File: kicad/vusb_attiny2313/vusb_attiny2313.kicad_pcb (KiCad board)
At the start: 2 copper layers, 38 parts, among them J1 USB, Q1 BSS138, Q2 BSS138, SW2 SW_DIP_x03, U1 74HC595, U2 ATTINY2313-20PU, U3 74HC595, U4 74HC595, U5 27C256, U6 LT1073CS, Y1 12Mhz

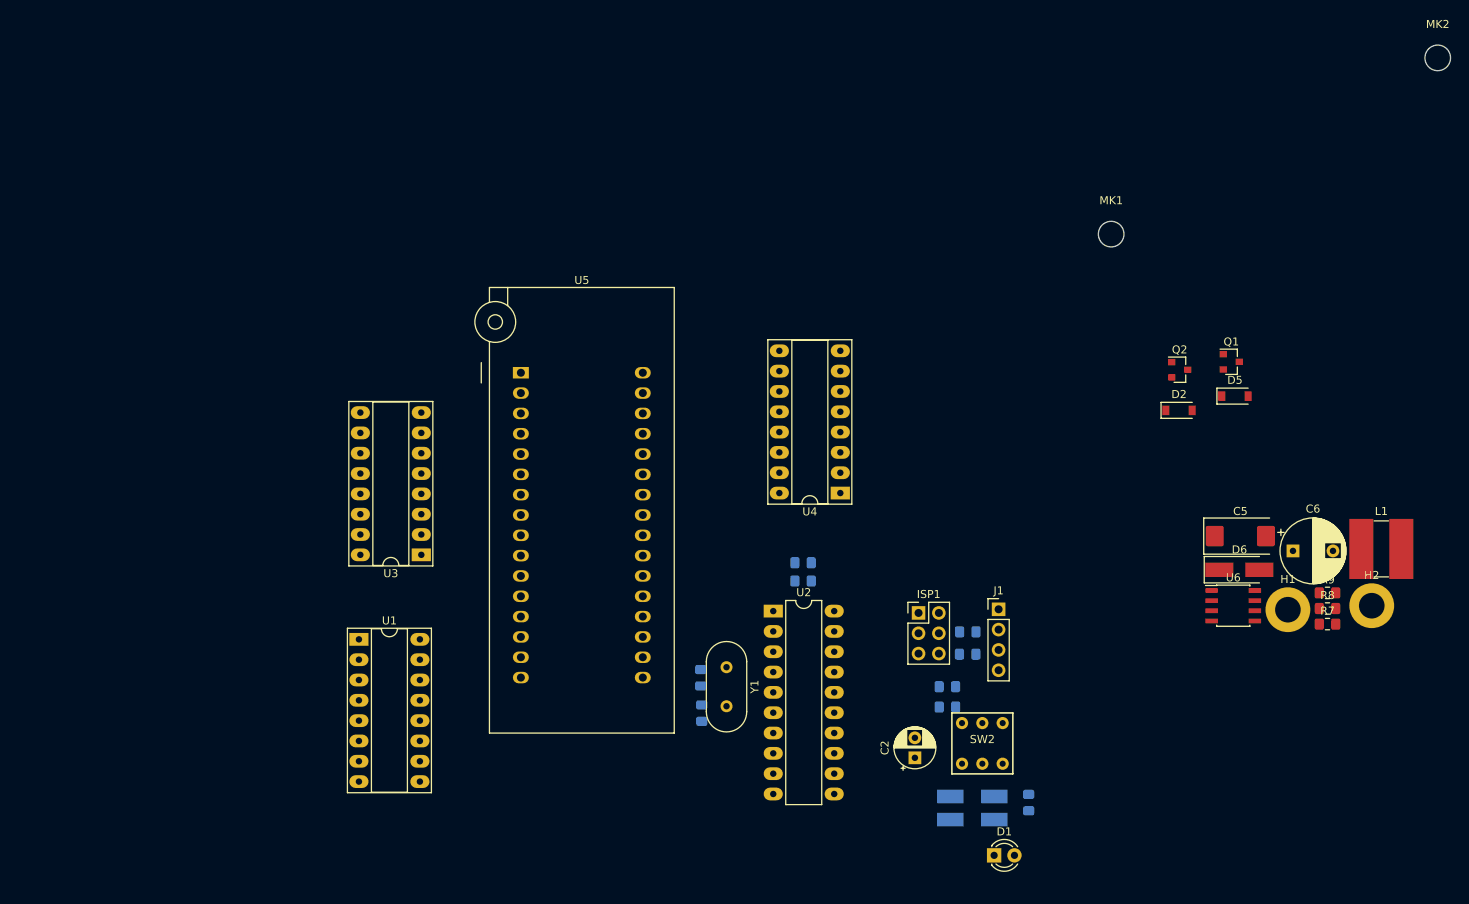
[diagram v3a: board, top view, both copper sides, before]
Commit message: fuses angepasst!
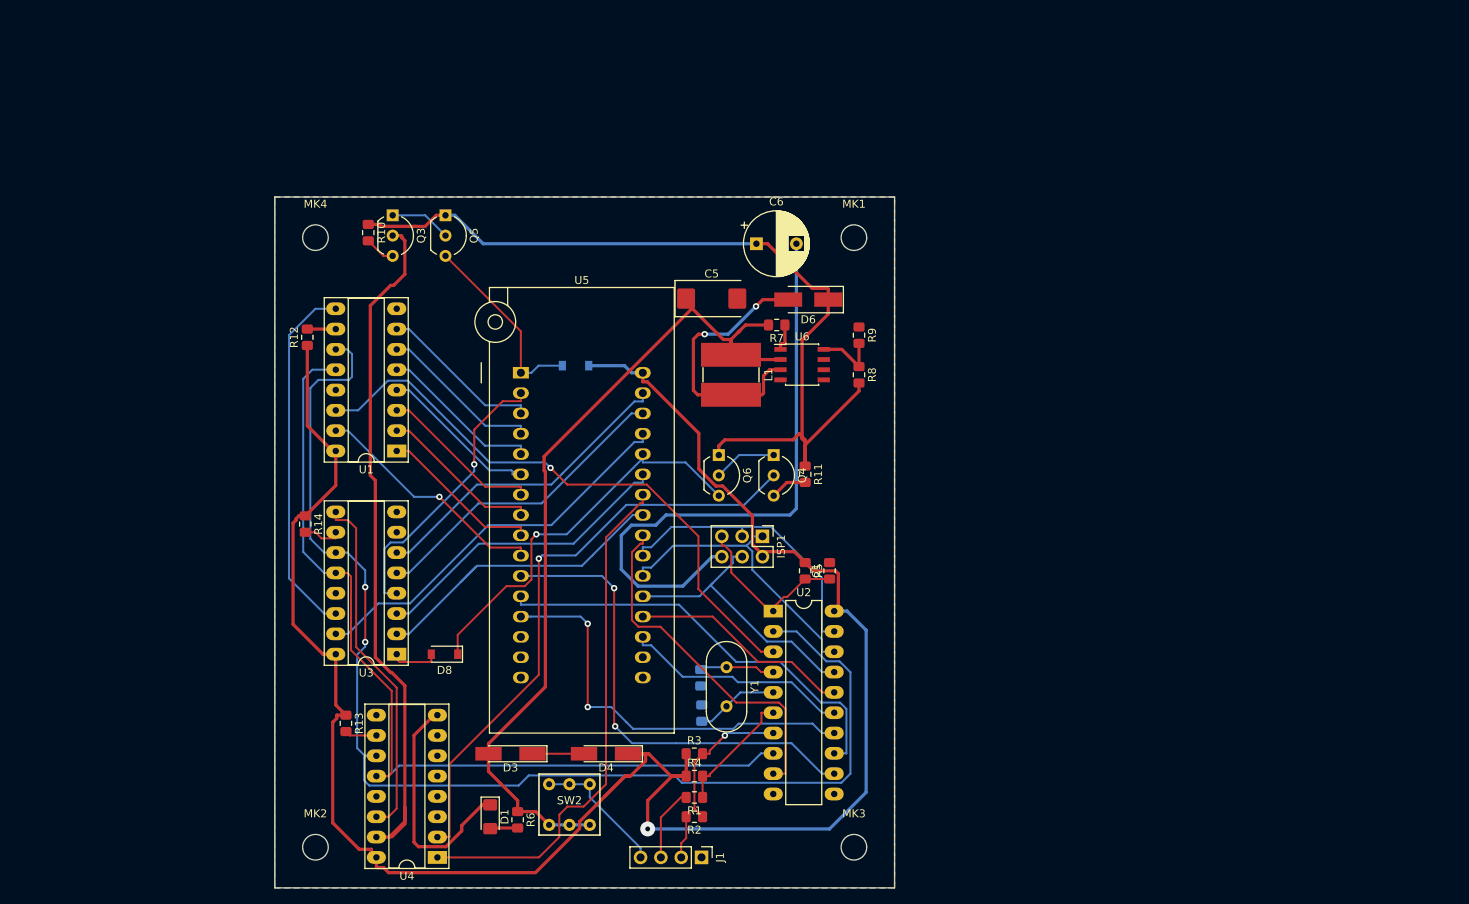
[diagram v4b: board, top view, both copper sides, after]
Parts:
- removed C2: 10µ, Capacitor_THT:CP_Radial_D5.0mm_P2.50mm
- removed D2, D5: SD 103BW, Diode_SMD:D_SOD-123
- removed H1, H2: MH, MountingHole:MountingHole_3.2mm_M3_DIN965_Pad
- removed Q1, Q2: BSS138, Package_TO_SOT_SMD:SOT-23
- added D7: SD 103BW, Diode_SMD:D_SOD-123, B.Cu at (99.8, 42.7)
- added D8: SD 103BW, Diode_SMD:D_SOD-123, F.Cu at (83.4, 78.7)
- added MK3: Mounting_Hole, MountingHole:MountingHole_3.2mm_M3, F.Cu at (134.6, 102.9)
- added MK4: Mounting_Hole, MountingHole:MountingHole_3.2mm_M3, F.Cu at (67.3, 26.7)
- added Q3: 2N3904, Package_TO_SOT_THT:TO-92_Inline_Wide, F.Cu at (77.0, 23.9)
- added Q4: 2N3904, Package_TO_SOT_THT:TO-92_Inline_Wide, F.Cu at (124.6, 53.8)
- added Q5: 2N3906, Package_TO_SOT_THT:TO-92_Inline_Wide, F.Cu at (83.6, 23.9)
- added Q6: 2N3906, Package_TO_SOT_THT:TO-92_Inline_Wide, F.Cu at (117.7, 53.8)
- added R10: 47k, Resistor_SMD:R_0805_2012Metric_Pad1.15x1.40mm_HandSolder, F.Cu at (73.9, 26.0)
- added R11: 47k, Resistor_SMD:R_0805_2012Metric_Pad1.15x1.40mm_HandSolder, F.Cu at (128.5, 56.3)
- added R12: 1k, Resistor_SMD:R_0805_2012Metric_Pad1.15x1.40mm_HandSolder, F.Cu at (66.3, 39.1)
- added R13: 1k, Resistor_SMD:R_0805_2012Metric_Pad1.15x1.40mm_HandSolder, F.Cu at (71.1, 87.4)
- added R14: 1k, Resistor_SMD:R_0805_2012Metric_Pad1.15x1.40mm_HandSolder, F.Cu at (66.0, 62.5)
- C1, D3, D4, R1, R2, R3, R4, R5, R6: moved to F.Cu
- D1: footprint LED_THT:LED_D3.0mm -> LED_SMD:LED_1206_3216Metric_Pad1.42x1.75mm_HandSolder
- moved MK2 171.5 mm to (67.3, 102.9)
- moved L1 84.2 mm to (119.3, 43.8), turned to 270 degrees
- moved R7 78.3 mm to (125.0, 37.6), turned to 180 degrees
- moved C6 77.3 mm to (122.4, 27.4)
- moved C5 72.4 mm to (116.8, 34.3)
- moved U4 67.9 mm to (82.5, 104.1)
- moved R9 66.8 mm to (135.3, 38.9), turned to 270 degrees
- moved R8 65.4 mm to (135.3, 43.8), turned to 270 degrees
- moved R6 63.9 mm to (92.6, 99.4)
- moved D6 63.6 mm to (128.9, 34.4), turned to 180 degrees
- moved D1 63.2 mm to (89.2, 99.1), turned to 270 degrees
- moved U6 61.7 mm to (128.1, 42.5)
- moved D3 58.0 mm to (91.7, 91.2), turned to 180 degrees
- moved SW2 52.2 mm to (99.1, 97.5)
- moved J1 48.4 mm to (115.6, 104.1), turned to 270 degrees
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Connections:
- net /DATA_Q renamed /Sheet5D4257EC/DATA_R
- U1 pad 1: /~CE -> Net-(U1-Pad1)
- U1 pad 10: /DATA_CLR -> Net-(R12-Pad2)
- U1 pad 14: /DATA_R -> /DATA_IN
- U1 pad 15: (no net) -> Net-(U1-Pad15)
- U1 pad 2: /~OE -> Net-(U1-Pad2)
- U1 pad 3: (no net) -> Net-(U1-Pad3)
- U1 pad 4: (no net) -> Net-(U1-Pad4)
- U1 pad 5: (no net) -> Net-(U1-Pad5)
- U1 pad 6: (no net) -> Net-(U1-Pad6)
- U1 pad 7: (no net) -> Net-(U1-Pad7)
- U1 pad 9: (no net) -> /Sheet5D4257EC/DATA_Q
- U3 pad 1: Net-(U3-Pad1) -> Net-(D8-Pad2)
- U3 pad 10: /DATA_CLR -> Net-(R14-Pad2)
- U3 pad 14: /DATA_IN -> /Sheet5D4257EC/DATA_Q
- U3 pad 15: Net-(U3-Pad15) -> /Sheet5D4257EC/A8
- U3 pad 2: Net-(U3-Pad2) -> /Sheet5D4257EC/A10
- U3 pad 3: Net-(U3-Pad3) -> /Sheet5D4257EC/A11
- U3 pad 4: Net-(U3-Pad4) -> /Sheet5D4257EC/A12
- U3 pad 5: Net-(U3-Pad5) -> /Sheet5D4257EC/A13
- U3 pad 6: Net-(U3-Pad6) -> /Sheet5D4257EC/A14
- U3 pad 7: Net-(U3-Pad7) -> (no net)
- U4 pad 1: /A9 -> /Sheet5D4257EC/~OE
- U4 pad 10: /DATA_CLR -> Net-(R13-Pad2)
- U4 pad 15: /A8 -> /Sheet5D4257EC/~VPP
- U4 pad 2: /A10 -> /Sheet5D4257EC/A9_
- U4 pad 3: /A11 -> (no net)
- U4 pad 4: /A12 -> (no net)
- U4 pad 5: /A13 -> (no net)
- U4 pad 6: /A14 -> (no net)
- U4 pad 9: /DATA_R -> (no net)
- U5 pad 1: /VPP -> /Sheet5D4257EC/VPP
- U5 pad 10: Net-(U3-Pad15) -> Net-(U1-Pad15)
- U5 pad 2: /A12 -> /Sheet5D4257EC/A12
- U5 pad 20: /~CE -> /DATA_CLR
- U5 pad 21: /A10 -> /Sheet5D4257EC/A10
- U5 pad 22: /~OE -> /Sheet5D4257EC/~OE
- U5 pad 23: /A11 -> /Sheet5D4257EC/A11
- U5 pad 24: /A9_ -> /Sheet5D4257EC/A9
- U5 pad 25: /A8 -> /Sheet5D4257EC/A8
- U5 pad 26: /A13 -> /Sheet5D4257EC/A13
- U5 pad 27: /A14 -> /Sheet5D4257EC/A14
- U5 pad 3: Net-(U3-Pad7) -> Net-(U1-Pad7)
- U5 pad 4: Net-(U3-Pad6) -> Net-(U1-Pad6)
- U5 pad 5: Net-(U3-Pad5) -> Net-(U1-Pad5)
- U5 pad 6: Net-(U3-Pad4) -> Net-(U1-Pad4)
- U5 pad 7: Net-(U3-Pad3) -> Net-(U1-Pad3)
- U5 pad 8: Net-(U3-Pad2) -> Net-(U1-Pad2)
- U5 pad 9: Net-(U3-Pad1) -> Net-(U1-Pad1)
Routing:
- net VCC: track 0.00 -> 253.6 mm, vias 0 -> 1
- net /DATA_SCK: track 0.00 -> 155.3 mm, vias 0 -> 2
- net /DATA_CS: track 0.00 -> 112.9 mm
- net +12V: track 0.00 -> 111.9 mm
- net +5V: track 0.00 -> 110.2 mm
- net GND: track 0.00 -> 105.2 mm
- net /Sheet5D4257EC/~VPP: track 0.00 -> 89.0 mm
- net /Sheet5D4257EC/A9_: track 0.00 -> 74.6 mm, vias 0 -> 1
- net /DATA_IN: track 0.00 -> 74.1 mm, vias 0 -> 1
- net /Sheet5D4257EC/~OE: track 0.00 -> 64.8 mm
- net /D0: track 0.00 -> 59.4 mm, vias 0 -> 2
- net /D1: track 0.00 -> 54.2 mm
- net /D2: track 0.00 -> 51.8 mm, vias 0 -> 2
- net /Sheet5D4257EC/A9: track 0.00 -> 49.9 mm, vias 0 -> 1
- net /Sheet5D4257EC/A8: track 0.00 -> 49.4 mm
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- added copper zone on B.Cu, net GND
- added copper zone on F.Cu, net GND
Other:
- board outline added: 77.5 x 86.4 mm
- net class signal: via_dia 1.562 -> 1.862; via_drill 0.4 -> 0.6
